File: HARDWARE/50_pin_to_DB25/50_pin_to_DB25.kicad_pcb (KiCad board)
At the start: 2 copper layers, 31.5 x 74.5 mm, 3 parts, among them J1 Conn_02x25_Odd_Even_MountingP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, J2 Conn_2Rows-25Pins_MountingPin

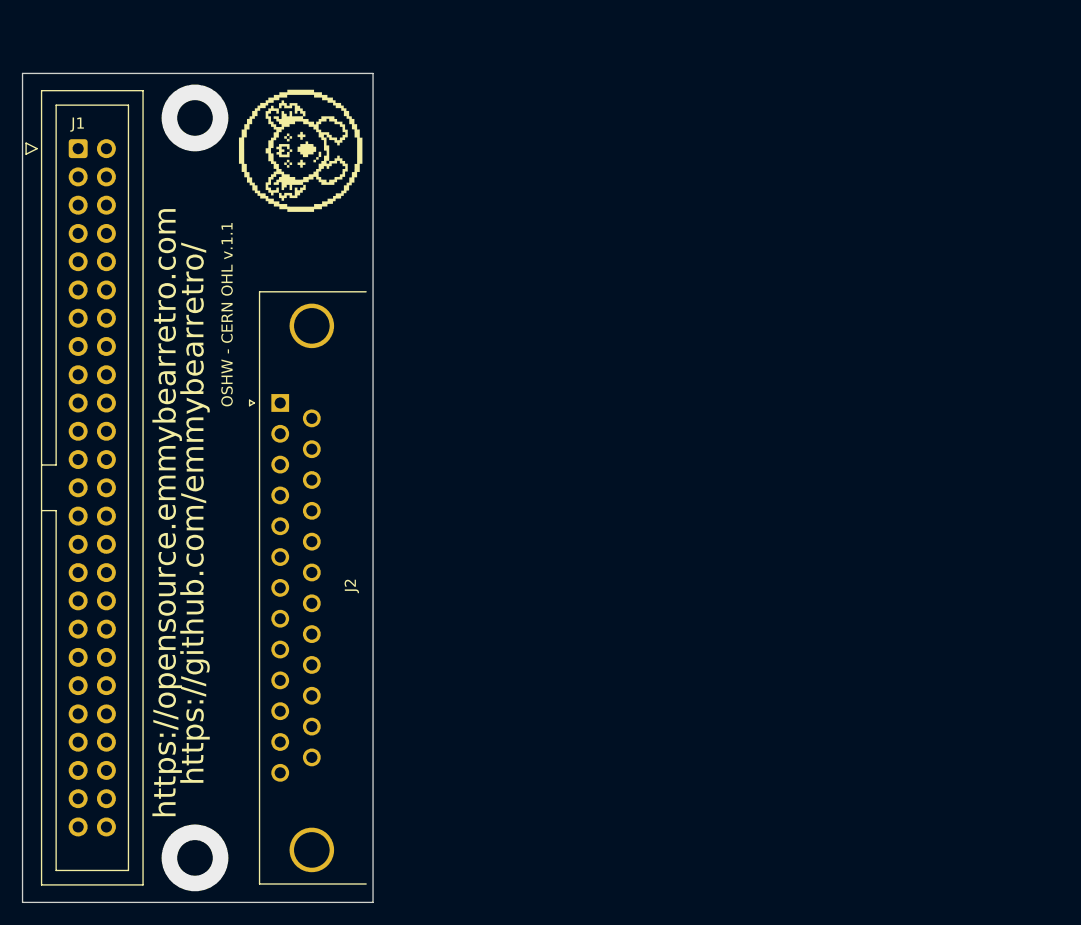
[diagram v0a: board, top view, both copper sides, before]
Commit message: routed wires
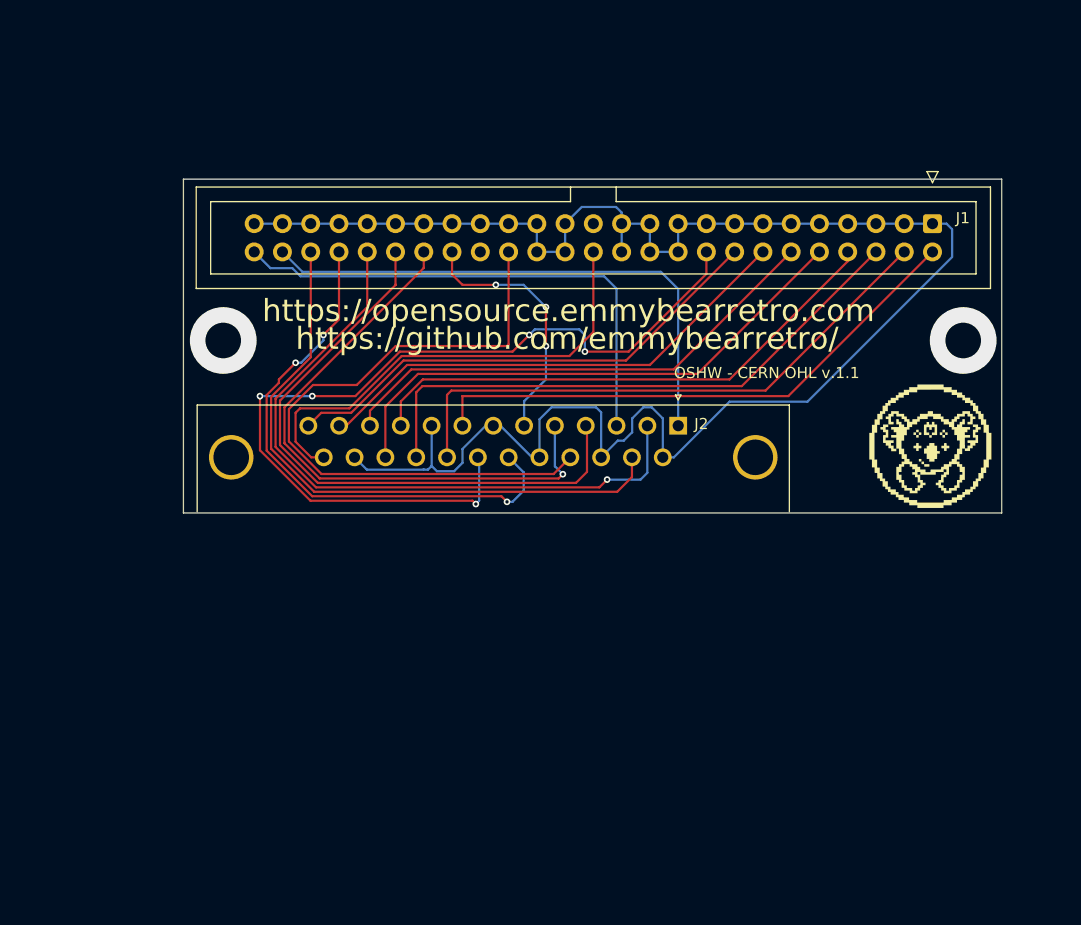
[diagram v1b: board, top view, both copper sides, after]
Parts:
- moved J1 77.1 mm to (94.8, 26.5), turned to -90 degrees
- moved G*** 62.4 mm to (94.5, 46.5), turned to 0 degrees
- moved J2 35.8 mm to (71.9, 44.7), turned to 0 degrees
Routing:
- net /DB25_PIN_GND: track 0.00 -> 165.2 mm
- net /DB25_PIN20 - DBP: track 0.00 -> 80.5 mm, vias 0 -> 5
- net /DB25_PIN2 - MSG: track 0.00 -> 60.9 mm, vias 0 -> 1
- net /DB25_PIN17 - ATN: track 0.00 -> 60.5 mm
- net /DB25_PIN15 - CD: track 0.00 -> 55.5 mm
- net /DB25_PIN4 - RST: track 0.00 -> 55.3 mm
- net /DB25_PIN5 - ACK: track 0.00 -> 53.9 mm, vias 0 -> 1
- net /DB25_PIN22 - DB2: track 0.00 -> 52.4 mm
- net /DB25_PIN21 - DB1: track 0.00 -> 52.0 mm
- net /DB25_PIN8 - DB0: track 0.00 -> 50.3 mm
- net /DB25_PIN19 - SEL: track 0.00 -> 49.8 mm, vias 0 -> 3
- net /DB25_PIN23 - DB4: track 0.00 -> 49.3 mm
- net /DB25_PIN1 - REQ: track 0.00 -> 49.2 mm
- net /DB25_PIN10 - DB3: track 0.00 -> 48.4 mm
- net /DB25_PIN3 - IO: track 0.00 -> 46.2 mm
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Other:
- board size 31.5 x 74.5 mm -> 73.5 x 30 mm
